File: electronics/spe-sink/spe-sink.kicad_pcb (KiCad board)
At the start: 4 copper layers, 38 x 65 mm, 80 parts, among them IC1 AT24C02C-SSHM, P1 CONN_01X03, Q1 2N7002P, U1 AP7375-33, U2 MCP65R41T, U3 ATL431LIB, U4 ADIN1110, U5 INA180A3, U6 AP2112K-3.3, X1 RH100-25.000-13-F-0715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

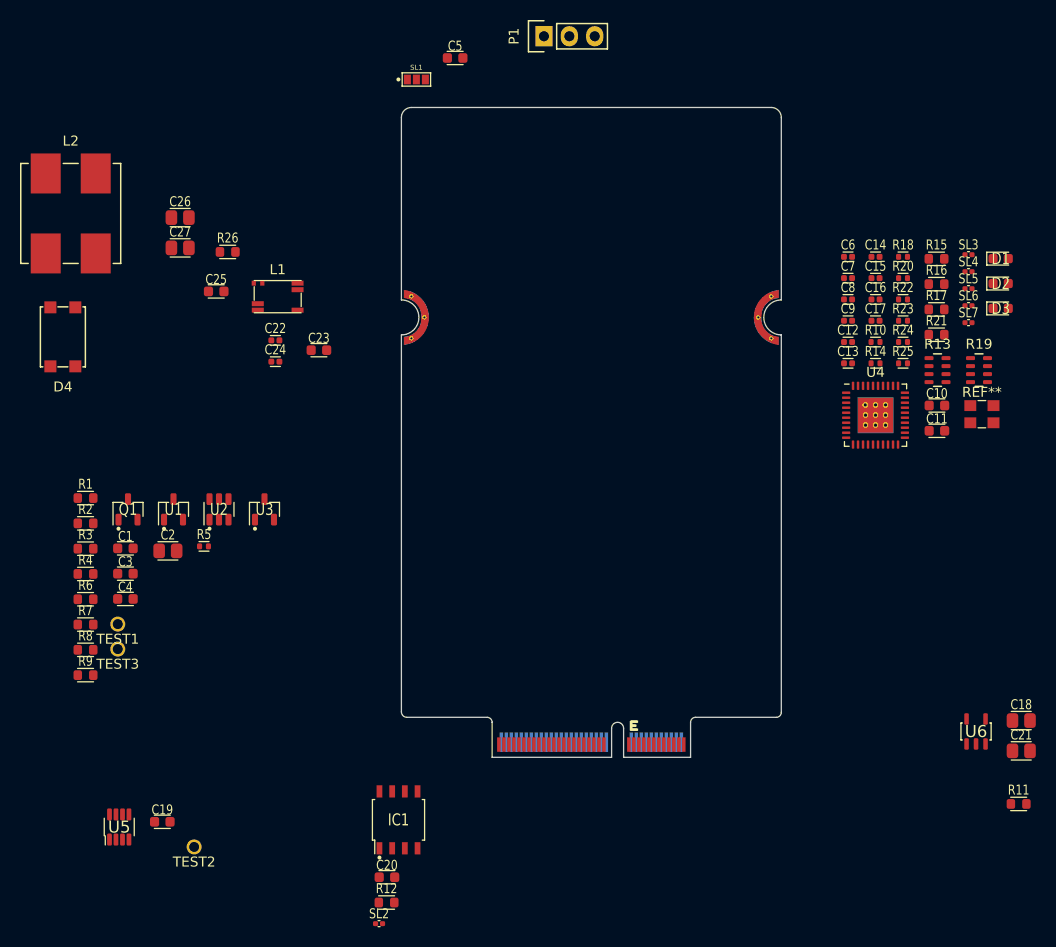
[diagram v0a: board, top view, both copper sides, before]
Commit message: PD function board bulk regulator, cleanup, part placement
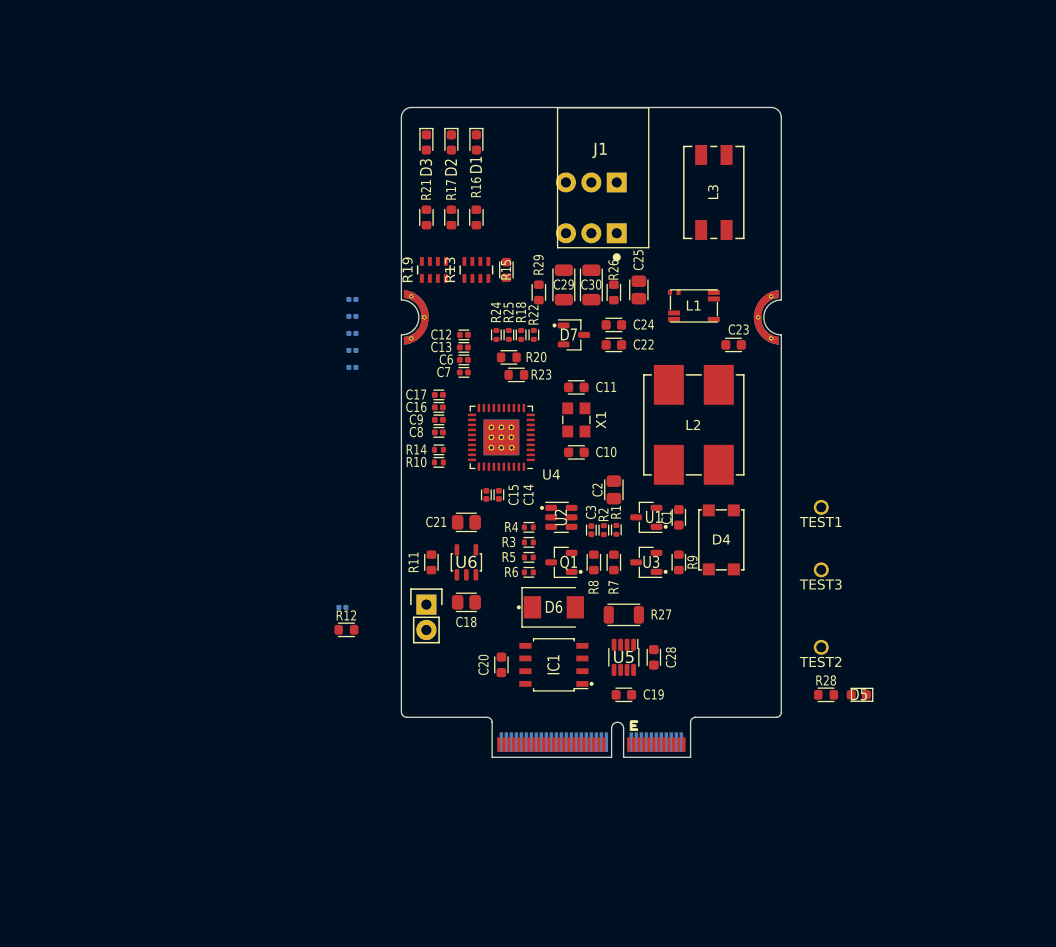
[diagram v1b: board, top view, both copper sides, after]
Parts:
- removed C26, C27: 470n_X7R_2012M_2, Applidyne_Capacitor:CAPC2012X110N
- removed C4: 100n_X7R_1608M, Applidyne_Capacitor:CAPC1608X90N
- removed C5: 4n7_X7R_1608M, Applidyne_Capacitor:CAPC1608X90N
- removed P1: CONN_01X03, Applidyne_Connector_Wurth:61300311121
- removed SL1: SOLDER-LINK-3, Applidyne_Link:SJ1608-3N
- added C28: 1n_X7R_1608M, Applidyne_Capacitor:CAPC1608X90N, F.Cu at (125.2, 94.0)
- added C29: 1n_X7R_3216M_2kV, Applidyne_Capacitor:CAPC3216X135N, F.Cu at (119.0, 56.8)
- added C30: 1n_X7R_3216M_2kV, Applidyne_Capacitor:CAPC3216X135N, F.Cu at (116.2, 56.8)
- added D5: LED_RED_1608M, Applidyne_LED:LEDC1608X80L40N, F.Cu at (145.8, 97.8)
- added D6: B240Q-13-F, Applidyne_SOD:SODFL5436X262N, F.Cu at (115.2, 89.0)
- added D7: D1213A, Applidyne_SOT:SOT95P240X110-3L16N, F.Cu at (117.2, 61.8)
- added J1: CONN_01X05_RA, Applidyne_Connector:CUI_TBL009-254-03, F.Cu at (121.5, 51.6)
- added L3: COMM_MODE_1000uH_800mA_0.3R, Applidyne_Inductor:WE-SL2, F.Cu at (131.2, 47.5)
- added P2: CONN_01X02, Applidyne_Connector_Wurth:61300211121, F.Cu at (102.5, 88.7)
- added R27: R01_3216M, Applidyne_Resistor:RESC3216X60N, F.Cu at (122.2, 89.8)
- added R28: 1K00_1608M, Applidyne_Resistor:RESC1608X50N, F.Cu at (142.5, 97.8)
- added R29: 1M_1608M, Applidyne_Resistor:RESC1608X50N, F.Cu at (113.8, 57.5)
- C22, C24: value 220n_X7R_1005M -> 220n_X7R_1608M; footprint Applidyne_Capacitor:CAPC1005X60N -> Applidyne_Capacitor:CAPC1608X90N
- C25: value 470n_X7R_1608M -> 470n_X7R_2012M_100V; footprint Applidyne_Capacitor:CAPC1608X90N -> Applidyne_Capacitor:CAPC2012X110N
- C3: value 330p_X7R_1608M -> 330p_X7R_1005M; footprint Applidyne_Capacitor:CAPC1608X90N -> Applidyne_Capacitor:CAPC1005X60N
- R1: value 1M_1608M -> 1M_1005M; footprint Applidyne_Resistor:RESC1608X50N -> Applidyne_Resistor:RESC1005X40N
- R2, R4: value 470K_1608M -> 470K_1005M; footprint Applidyne_Resistor:RESC1608X50N -> Applidyne_Resistor:RESC1005X40N
- R20, R23: value 10K2_1005M -> 10K2_1608M; footprint Applidyne_Resistor:RESC1005X40N -> Applidyne_Resistor:RESC1608X50N
- R3: value 10K0_1608M -> 10K0_1005M; footprint Applidyne_Resistor:RESC1608X50N -> Applidyne_Resistor:RESC1005X40N
- R6: value 100K_1608M -> 10K0_1005M; footprint Applidyne_Resistor:RESC1608X50N -> Applidyne_Resistor:RESC1005X40N
- SL2, SL3, SL4, SL5, SL6, SL7: moved to B.Cu
- moved TEST1 71.3 mm to (142.0, 79.0)
- moved TEST3 70.8 mm to (142.0, 85.2)
- moved D4 68.9 mm to (132.0, 82.2), turned to 180 degrees
- moved TEST2 65.8 mm to (142.0, 93.0)
- moved L2 65.8 mm to (129.2, 70.8), turned to 180 degrees
- moved R11 63.5 mm to (103.0, 84.5), turned to 90 degrees
- moved SL3 61.8 mm to (95.1, 58.2), turned to 180 degrees
- moved SL4 61.8 mm to (95.1, 59.9), turned to 180 degrees
- moved SL5 61.8 mm to (95.1, 61.6), turned to 180 degrees
- moved SL6 61.8 mm to (95.1, 63.3), turned to 180 degrees
- moved SL7 61.8 mm to (95.1, 65.0), turned to 180 degrees
- moved R9 60.4 mm to (127.8, 84.5), turned to -90 degrees
- moved C21 60.0 mm to (106.5, 80.5)
- moved D3 59.8 mm to (102.5, 42.5), turned to -90 degrees
- moved C18 56.7 mm to (106.5, 88.5)
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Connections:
- C1 pad 1: Net-(TEST3-PAD) -> /PoDL Device Handling/PoDL+
- C18 pad 1: Net-(U6-VIN) -> +POWER
- D4 pad 1: unconnected-(D4-+-Pad1) -> /PoDL Device Handling/PoDL+
- L1 pad 6: Net-(C26-Pad2) -> Net-(L1-Pad6)
- L1 pad 7: Net-(C27-Pad2) -> Net-(L1-Pad7)
- L2 pad 2: Net-(C26-Pad1) -> Net-(L1-Pad6)
- L2 pad 3: Net-(C27-Pad1) -> Net-(L1-Pad7)
- R1 pad 1: Net-(TEST3-PAD) -> /PoDL Device Handling/PoDL+
- R11 pad 1: Net-(U6-VIN) -> +POWER
- R26 pad 2: unconnected-(R26-Pad2) -> Net-(C29-Pad1)
- R9 pad 1: Net-(TEST3-PAD) -> /PoDL Device Handling/PoDL+
- TEST2 pad 1: Net-(TEST2-PAD) -> /MicroMod Function Board/ANALOG
- TEST3 pad 1: Net-(TEST3-PAD) -> /PoDL Device Handling/PoDL+
- U1 pad 1: Net-(TEST3-PAD) -> /PoDL Device Handling/PoDL+
- U4 pad 41: (no net) -> GND
- U5 pad 1: Net-(TEST2-PAD) -> /MicroMod Function Board/ANALOG
- U5 pad 3: unconnected-(U5-S+-Pad3) -> Net-(U5-S+)
- U5 pad 4: unconnected-(U5-S--Pad4) -> Net-(U5-S-)
- U6 pad 1: Net-(U6-VIN) -> +POWER
- X2 pad 72: unconnected-(X2-VCC-Pad72) -> +POWER
- X2 pad 73: unconnected-(X2-3V3-Pad73) -> +3.3V_MCU
- X2 pad 74: unconnected-(X2-VCC-Pad74) -> +POWER

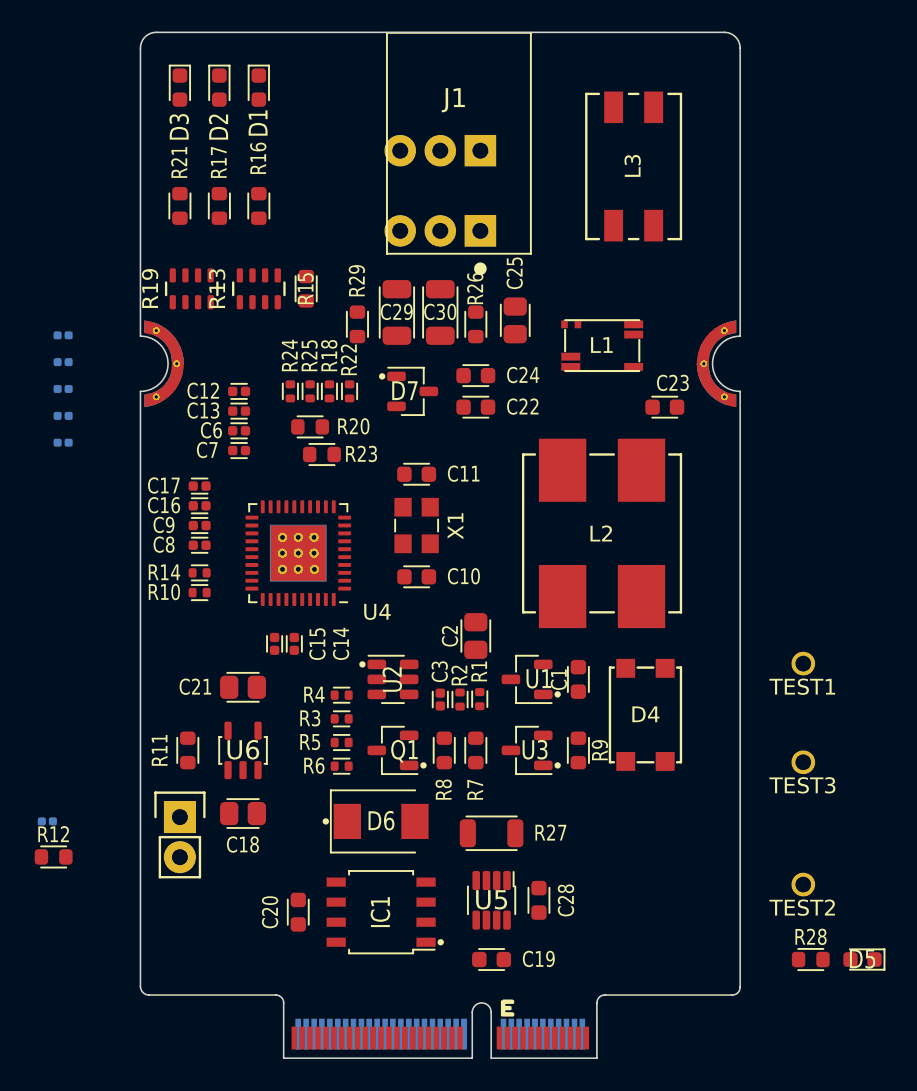
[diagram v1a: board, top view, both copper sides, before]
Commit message: PD sink board routing, minor sch changes, etc
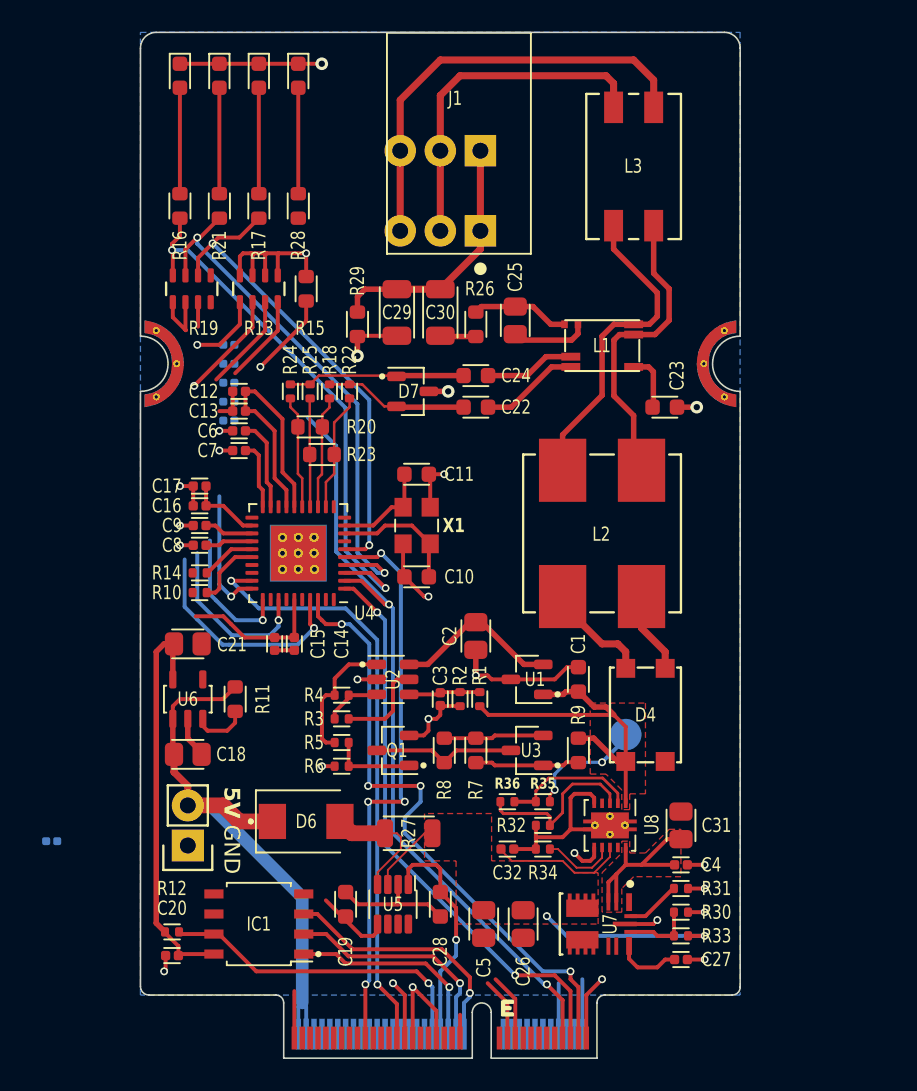
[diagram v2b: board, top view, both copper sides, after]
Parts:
- removed TEST2: CLIP_HOOK_BLUE, Applidyne_Test:KEYSTONE_5117
- removed TEST3: CLIP_HOOK_GREY, Applidyne_Test:KEYSTONE_5118
- added C26: 22u_X5R_2012M, Applidyne_Capacitor:CAPC2012X110N, F.Cu at (124.2, 95.5)
- added C27: 1u_X5R_1005M, Applidyne_Capacitor:CAPC1005X60N, F.Cu at (134.2, 97.8)
- added C31: 10u_X5R_2012M_50V, Applidyne_Capacitor:CAPC2012X110N, F.Cu at (134.2, 89.2)
- added C32: 10n_X7R_1005M, Applidyne_Capacitor:CAPC1005X60N, F.Cu at (123.2, 90.8)
- added C4: 100n_X7R_1005M, Applidyne_Capacitor:CAPC1005X60N, F.Cu at (134.2, 91.8)
- added C5: 22u_X5R_2012M, Applidyne_Capacitor:CAPC2012X110N, F.Cu at (121.8, 95.5)
- added R30: 10K0_1005M, Applidyne_Resistor:RESC1005X40N, F.Cu at (134.2, 94.8)
- added R31: 15K_1005M, Applidyne_Resistor:RESC1005X40N, F.Cu at (134.2, 93.2)
- added R32: 26K1_1005M, Applidyne_Resistor:RESC1005X40N, F.Cu at (125.5, 89.2)
- added R33: 40K2_1005M, Applidyne_Resistor:RESC1005X40N, F.Cu at (134.2, 96.2)
- added R34: 13K_1005M, Applidyne_Resistor:RESC1005X40N, F.Cu at (125.5, 90.8)
- added R35: 680K_1005M, Applidyne_Resistor:RESC1005X40N, F.Cu at (125.5, 87.8)
- added R36: 36K_1005M, Applidyne_Resistor:RESC1005X40N, F.Cu at (123.2, 87.8)
- added U7: TLVM23625RDNR, Applidyne_QFN:QFN50P450X350X200-11-FCMOD11, F.Cu at (129.0, 95.5)
- added U8: TPS26625, Applidyne_SON:SON50P300X300X90-11T240X165N_RELIEF, F.Cu at (129.8, 89.2)
- C20: value 100n_X7R_1608M -> 100n_X7R_1005M; footprint Applidyne_Capacitor:CAPC1608X90N -> Applidyne_Capacitor:CAPC1005X60N
- R12: value 100K_1608M -> 100K_1005M; footprint Applidyne_Resistor:RESC1608X50N -> Applidyne_Resistor:RESC1005X40N
- TEST1: value CLIP_HOOK_ORANGE -> PROBE_PAD; footprint Applidyne_Test:KEYSTONE_5003 -> Applidyne_Test:TP200; moved to B.Cu
- moved D5 66.4 mm to (110.0, 41.8), turned to -90 degrees
- moved R28 57.7 mm to (110.0, 50.0), turned to 90 degrees
- moved TEST1 12.1 mm to (130.8, 83.5), turned to 180 degrees
- moved SL4 11.1 mm to (105.6, 63.6), turned to 0 degrees
- moved SL7 10.8 mm to (105.6, 62.4), turned to 0 degrees
- moved SL6 10.7 mm to (105.6, 61.2), turned to 0 degrees
- moved SL5 10.6 mm to (105.6, 60.0), turned to 0 degrees
- moved SL3 10.5 mm to (105.6, 58.8), turned to 0 degrees
- moved C19 9.89 mm to (113.0, 94.2), turned to 90 degrees
- moved R12 8.88 mm to (102.0, 96.0)
- moved C20 8.46 mm to (102.0, 97.5), turned to 180 degrees
- moved IC1 7.79 mm to (107.5, 95.5)
- moved C28 6.25 mm to (119.0, 94.2)
- moved U5 6.25 mm to (116.0, 94.2)
- moved R27 5.25 mm to (117.0, 89.8)
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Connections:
- C2 pad 1: Net-(TEST1-PAD) -> Net-(U1-VOUT)
- R19 pad 6: Net-(U4-LINK_ST) -> Net-(U4-LED_1)
- R19 pad 7: Net-(U4-LED_1) -> Net-(U4-LINK_ST)
- TEST1 pad 1: Net-(TEST1-PAD) -> /PoDL Device Handling/PoDL+
- U1 pad 2: Net-(TEST1-PAD) -> Net-(U1-VOUT)
- U2 pad 6: Net-(TEST1-PAD) -> Net-(U1-VOUT)
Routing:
- net GND: track 0.00 -> 95.4 mm, vias 0 -> 24
- net +3.3V: track 0.00 -> 73.5 mm, vias 0 -> 1
- net /Ethernet MAC+PHY/CIPO: track 0.00 -> 49.6 mm, vias 0 -> 2
- net /Ethernet MAC+PHY/CLK: track 0.00 -> 39.4 mm, vias 0 -> 4
- net /Ethernet MAC+PHY/~{CS}: track 0.00 -> 37.9 mm, vias 0 -> 2
- net +POWER: track 0.00 -> 37.4 mm
- net /Ethernet MAC+PHY/~{RESET}: track 0.00 -> 36.2 mm, vias 0 -> 4
- net /Ethernet MAC+PHY/COPI: track 0.00 -> 36.2 mm, vias 0 -> 2
- net Net-(U4-LED_0): track 0.00 -> 34.6 mm, vias 0 -> 2
- net Net-(U4-LINK_ST): track 0.00 -> 33.8 mm, vias 0 -> 2
- net /PoDL Device Handling/PoDL+: track 0.00 -> 31.0 mm, vias 0 -> 2
- net Net-(U4-LED_1): track 0.00 -> 30.9 mm, vias 0 -> 2
- net Net-(J1-Pin_3): track 0.00 -> 27.7 mm
- net Net-(J1-Pin_2): track 0.00 -> 21.8 mm
- net Net-(IC1-WP): track 0.00 -> 20.5 mm, vias 0 -> 1
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- added copper zone on F.Cu, net /PoDL Device Handling/PoDL+
- added copper zone on B.Cu, net GND
- added copper zone on F.Cu, net Net-(U5-S+)
- added copper zone on F.Cu, net Net-(U7-EN)
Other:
- board text added: "5V"
- board text added: "GND"

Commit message: PD sink PCB design 'finished', page cleanup, etc
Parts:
- C19: value 100n_X7R_1608M -> 100n_X7R_1005M; footprint Applidyne_Capacitor:CAPC1608X90N -> Applidyne_Capacitor:CAPC1005X60N
- C28: value 1n_X7R_1608M -> 1n_X7R_1005M; footprint Applidyne_Capacitor:CAPC1608X90N -> Applidyne_Capacitor:CAPC1005X60N
- moved R15 21.2 mm to (121.3, 73.5)
- moved SL4 18.7 mm to (119.6, 76.0)
- moved SL2 12.9 mm to (105.6, 96.6)
- moved D1 5.00 mm to (107.5, 41.8)
- moved D2 5.00 mm to (102.5, 41.8)
- moved R16 5.00 mm to (107.5, 50.0)
- moved R17 5.00 mm to (102.5, 50.0)
- moved SL5 2.40 mm to (105.6, 62.4)
- moved SL6 1.20 mm to (105.6, 60.0)
- moved SL7 1.20 mm to (105.6, 61.2)
- moved C19 0.75 mm to (113.8, 94.2)
- moved U5 0.50 mm to (116.5, 94.2)
- moved C28 0.25 mm to (119.2, 94.2)
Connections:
- R19 pad 6: Net-(U4-LED_1) -> Net-(U4-LED_0)
- R19 pad 8: Net-(U4-LED_0) -> Net-(U4-LED_1)
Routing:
- net Net-(U5-S-): track 7.88 -> 66.0 mm, vias 0 -> 2
- net /Ethernet MAC+PHY/~{INT}: track 7.27 -> 43.0 mm, vias 1 -> 2
- net +3.3V: track 73.5 -> 103.7 mm, vias 1 -> 0
- net /MicroMod Function Board/SDA: track 4.24 -> 25.8 mm
- net Net-(U4-SPI_CFG1): track 14.5 -> 35.4 mm
- net /MicroMod Function Board/SCL: track 3.99 -> 23.8 mm
- net GND: track 95.4 -> 115.0 mm, vias 24 -> 43
- net Net-(U4-~{SWPD_EN}): track 11.0 -> 29.9 mm
- net Net-(U4-~{TX2P4_EN}): track 8.75 -> 26.2 mm
- net Net-(U4-TS_TIMER/MS_SEL): track 8.18 -> 19.9 mm
- net /Ethernet MAC+PHY/CIPO: track 49.6 -> 38.2 mm
- net Net-(U4-LED_1): track 30.9 -> 40.5 mm
- net Net-(U5-S+): track 16.3 -> 25.4 mm
- net Net-(U4-LED_0): track 34.6 -> 41.2 mm
- net Net-(U4-LINK_ST): track 33.8 -> 40.1 mm
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- added copper zone on F.Cu, net +3.3V
- added copper zone on F.Cu, net GND
- added copper zone on B.Cu, net Net-(U8-EP)
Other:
- copper layers 4 -> 2
- board text added: "2 Layer 0.8mm >TG135 1oz copper layers 64 x 38 mm If available, chamfer edge connector Red soldermask White silkscreen ENIG finish recommended"
- board text added: "EEPROM WP"
- board text added: "JLCJLCJLCJLC"
- board text added: "LED0"
- board text added: "LED1"
- board text added: "LINK"
- board text added: "Manufacturing Notes"
- board text added: "PoDL"
- board text added: "PoDL RAW"
- board text added: "SINGLE PAIR ETHERNET MICROMOD FUNCTION BOARD PoDL CLASS 10|11|12"
- board text added: "SPI CFG0"
- board text added: "SPI CFG1 SW PWR CTL TX 1V ONLY MASTER SEL"
- board text added: "V1.0 S.RAPSON 2023"

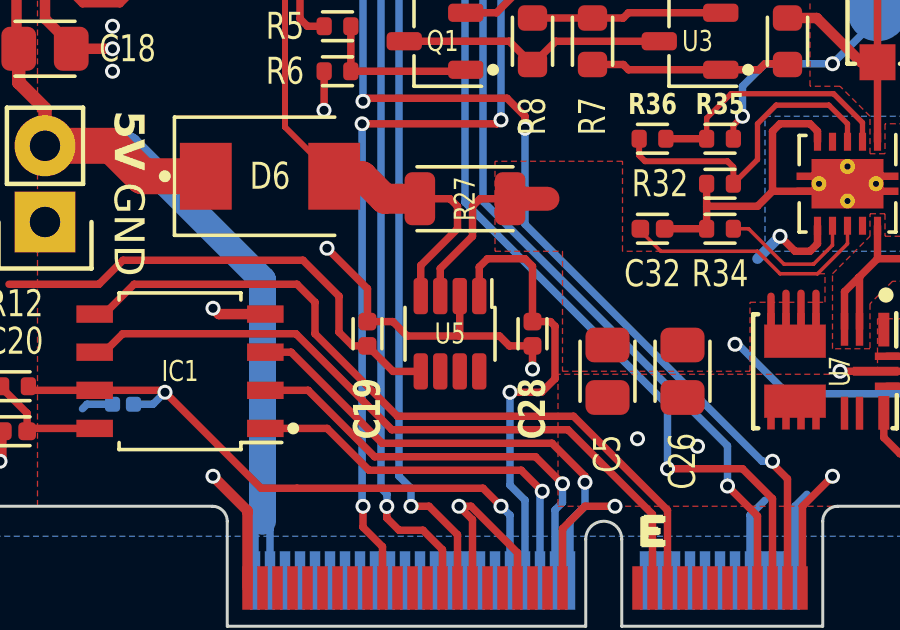
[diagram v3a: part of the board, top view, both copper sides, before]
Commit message: Fix current amplifier part choice on PD board
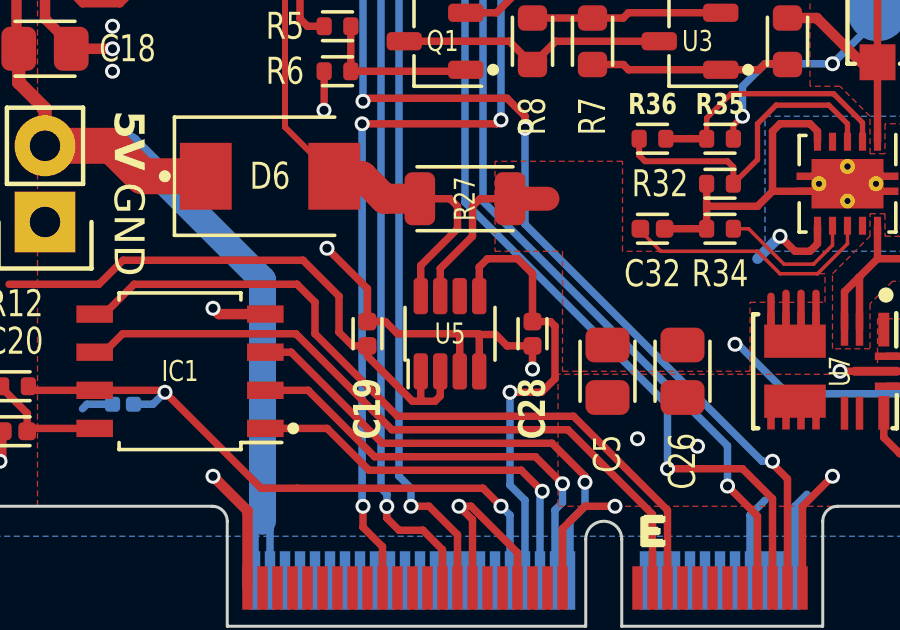
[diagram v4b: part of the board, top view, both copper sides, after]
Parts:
- U5: value INA180A3 -> INA186A3
- turned U5 to 0 degrees
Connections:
- U5 pad 1: /MicroMod Function Board/ANALOG -> +3.3V
- U5 pad 2: GND -> +3.3V
- U5 pad 3: Net-(U5-S+) -> GND
- U5 pad 4: Net-(U5-S-) -> GND
- U5 pad 5: +3.3V -> /MicroMod Function Board/ANALOG
- U5 pad 6: (no net) -> unconnected-(U5-NC-Pad6)
- U5 pad 7: (no net) -> Net-(U5-S+)
- U5 pad 8: (no net) -> Net-(U5-S-)
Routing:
- net +3.3V: track 103.7 -> 106.8 mm
- net GND: track 115.0 -> 116.2 mm
